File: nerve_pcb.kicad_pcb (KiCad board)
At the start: 6 copper layers, 50 x 50 mm, 72 parts, among them J1 TC2050-IDC, J2 2171750001, J4 472192001, J5 2x8, J6 2x15, J7 CAN1, J8 CAN2, SW1 SPST, SW2 SPST, U1 ld39150dt33-r, U2 STM32F446RET, U3 BNO085, U4 BMP390, U5 TJA1051T/3, U6 TJA1051T/3, Y1 8M, Y2 32k768, Y3 32k768

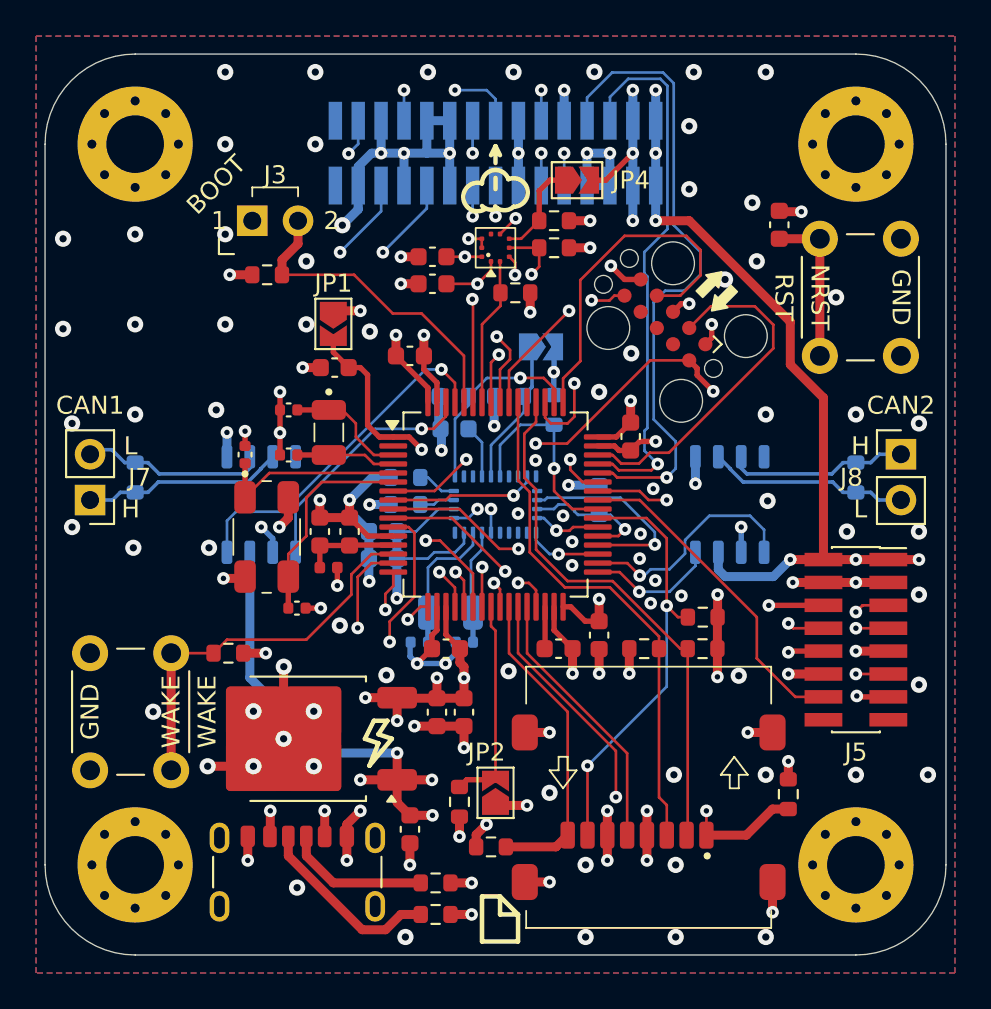
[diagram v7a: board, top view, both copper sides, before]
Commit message: Update J5 2x8 GPS connector
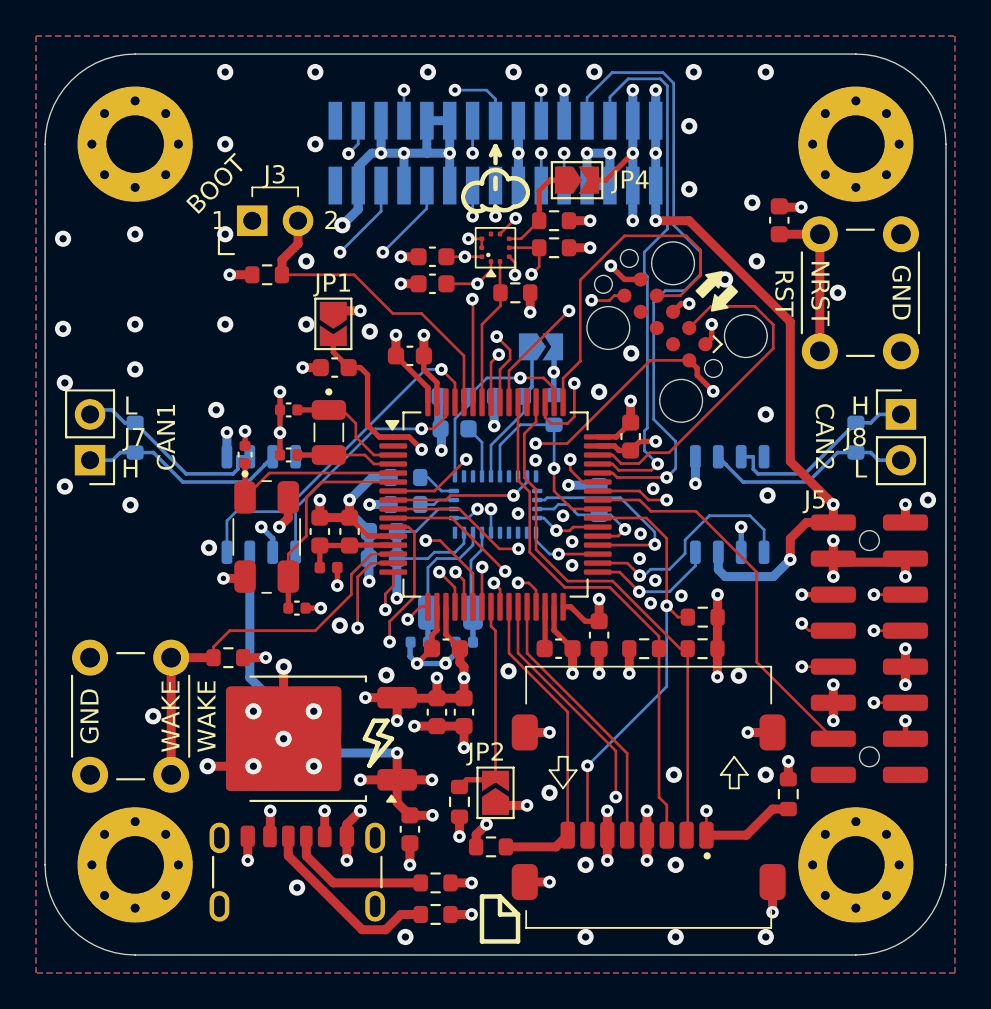
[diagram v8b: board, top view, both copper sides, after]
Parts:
- J5: value 2x8 -> BF030-16A-B1-0360-0277-0600-LB; footprint Connector_PinSocket_1.27mm:PinSocket_2x08_P1.27mm_Vertical_SMD -> connectors:bf030-16a-b1-0360-0277-0600-lb
- moved J7 2.21 mm to (126.0, 102.5)
- moved J8 2.21 mm to (171.0, 100.0)
- moved R20 2.21 mm to (128.5, 101.3)
- moved R21 2.21 mm to (168.5, 101.3)
- moved J5 0.90 mm to (169.2, 113.0), turned to -90 degrees
- moved C11 0.25 mm to (164.2, 89.2)
- moved SW1 0.25 mm to (171.0, 90.0)
- moved R3 0.25 mm to (133.7, 113.5)
- moved SW2 0.25 mm to (130.5, 113.5)
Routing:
- net +5V: track 72.3 -> 68.2 mm
- net /TIM1_CH1_PWM: track 18.4 -> 21.5 mm
- net +3.3VBATT: track 45.0 -> 47.4 mm
- net +3V3: track 87.0 -> 88.9 mm, vias 35 -> 36
- net /USART2_RX: track 29.1 -> 30.3 mm
- net /nerve_pcb_can/CAN2+: track 11.1 -> 12.0 mm
- net /nerve_pcb_can/CAN1-: track 10.2 -> 11.1 mm
- net /GPIO_GPS_RST: track 36.3 -> 37.2 mm
- net /USART2_TX: track 31.6 -> 32.5 mm
- net /PC3: track 32.3 -> 33.1 mm
- net /PC1: track 26.6 -> 27.4 mm
- net /PC2: track 26.4 -> 27.0 mm
- net GND: track 129.3 -> 129.6 mm, vias 131 -> 126
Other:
- board text removed: "120R"
